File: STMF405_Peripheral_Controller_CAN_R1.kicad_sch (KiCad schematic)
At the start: 169 parts, among them J1 10155435-00011LF, SW1 EVP-AA602W, U1 AP63205WU, U2 AP63203WU, U3 STM32F405RGTx, U4 TJA1051TK-3, Y1 8MHz

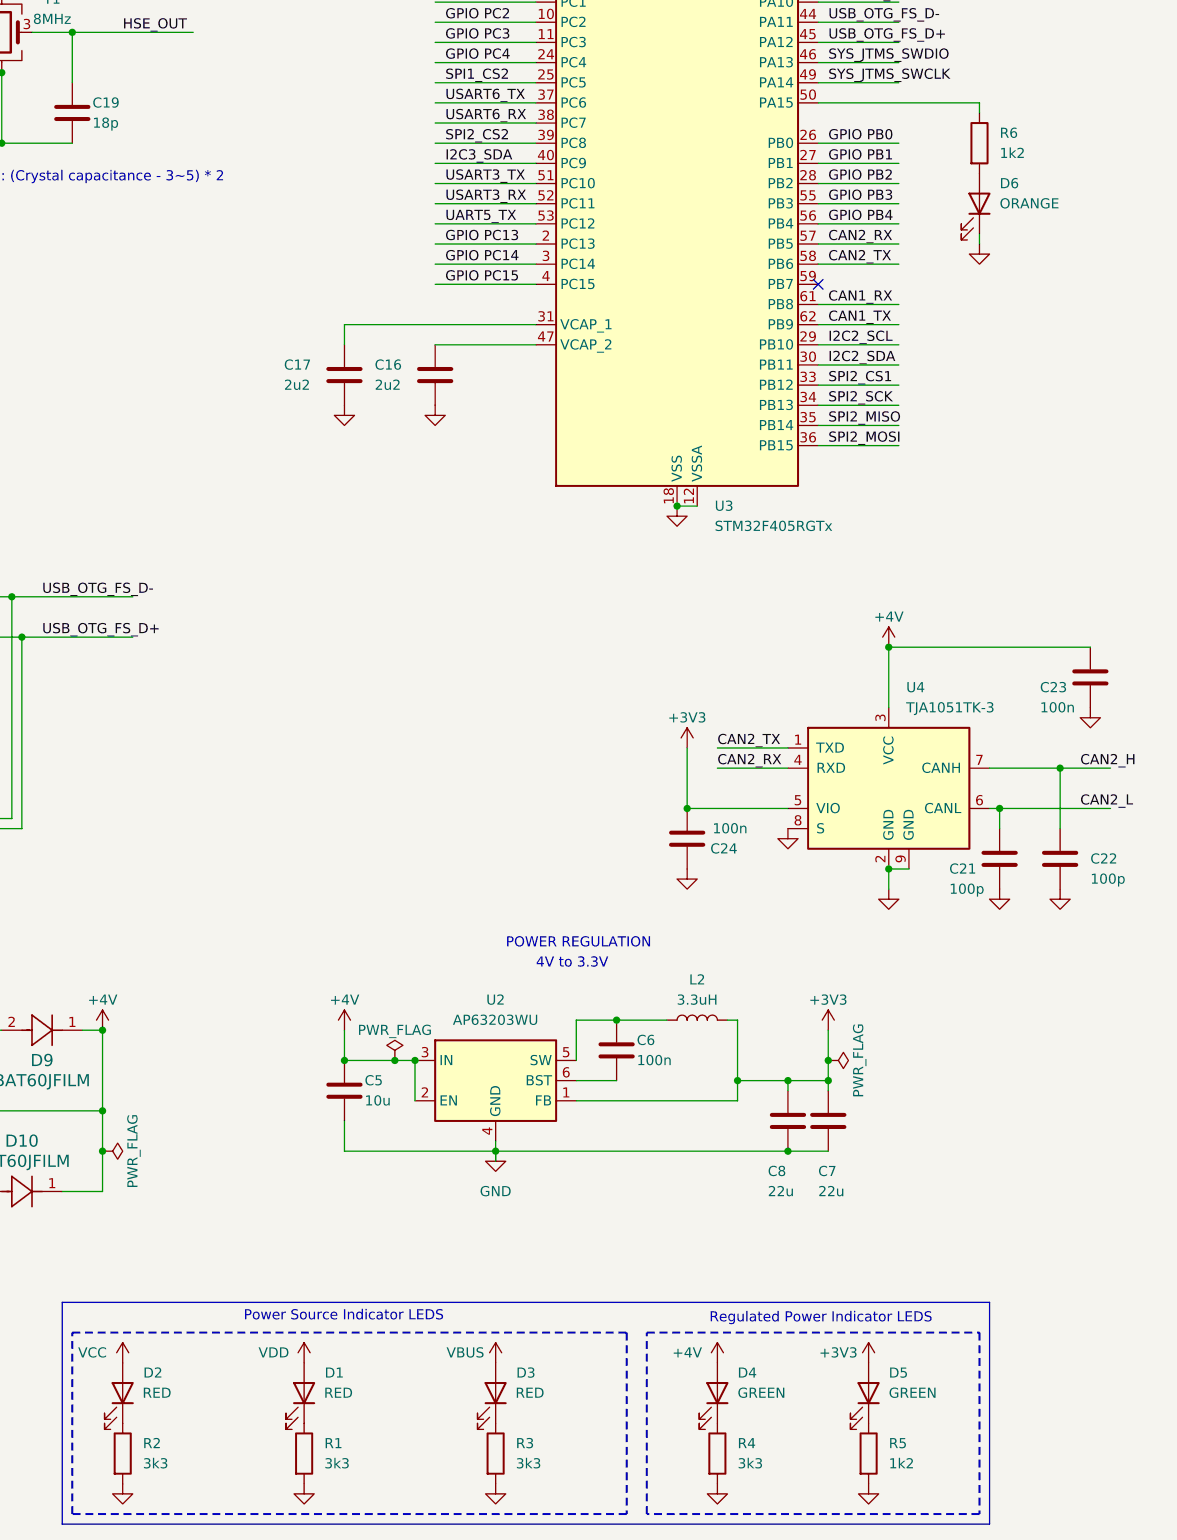
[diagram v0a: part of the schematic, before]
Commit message: cleanup resistors for LEDs, check rules and layout
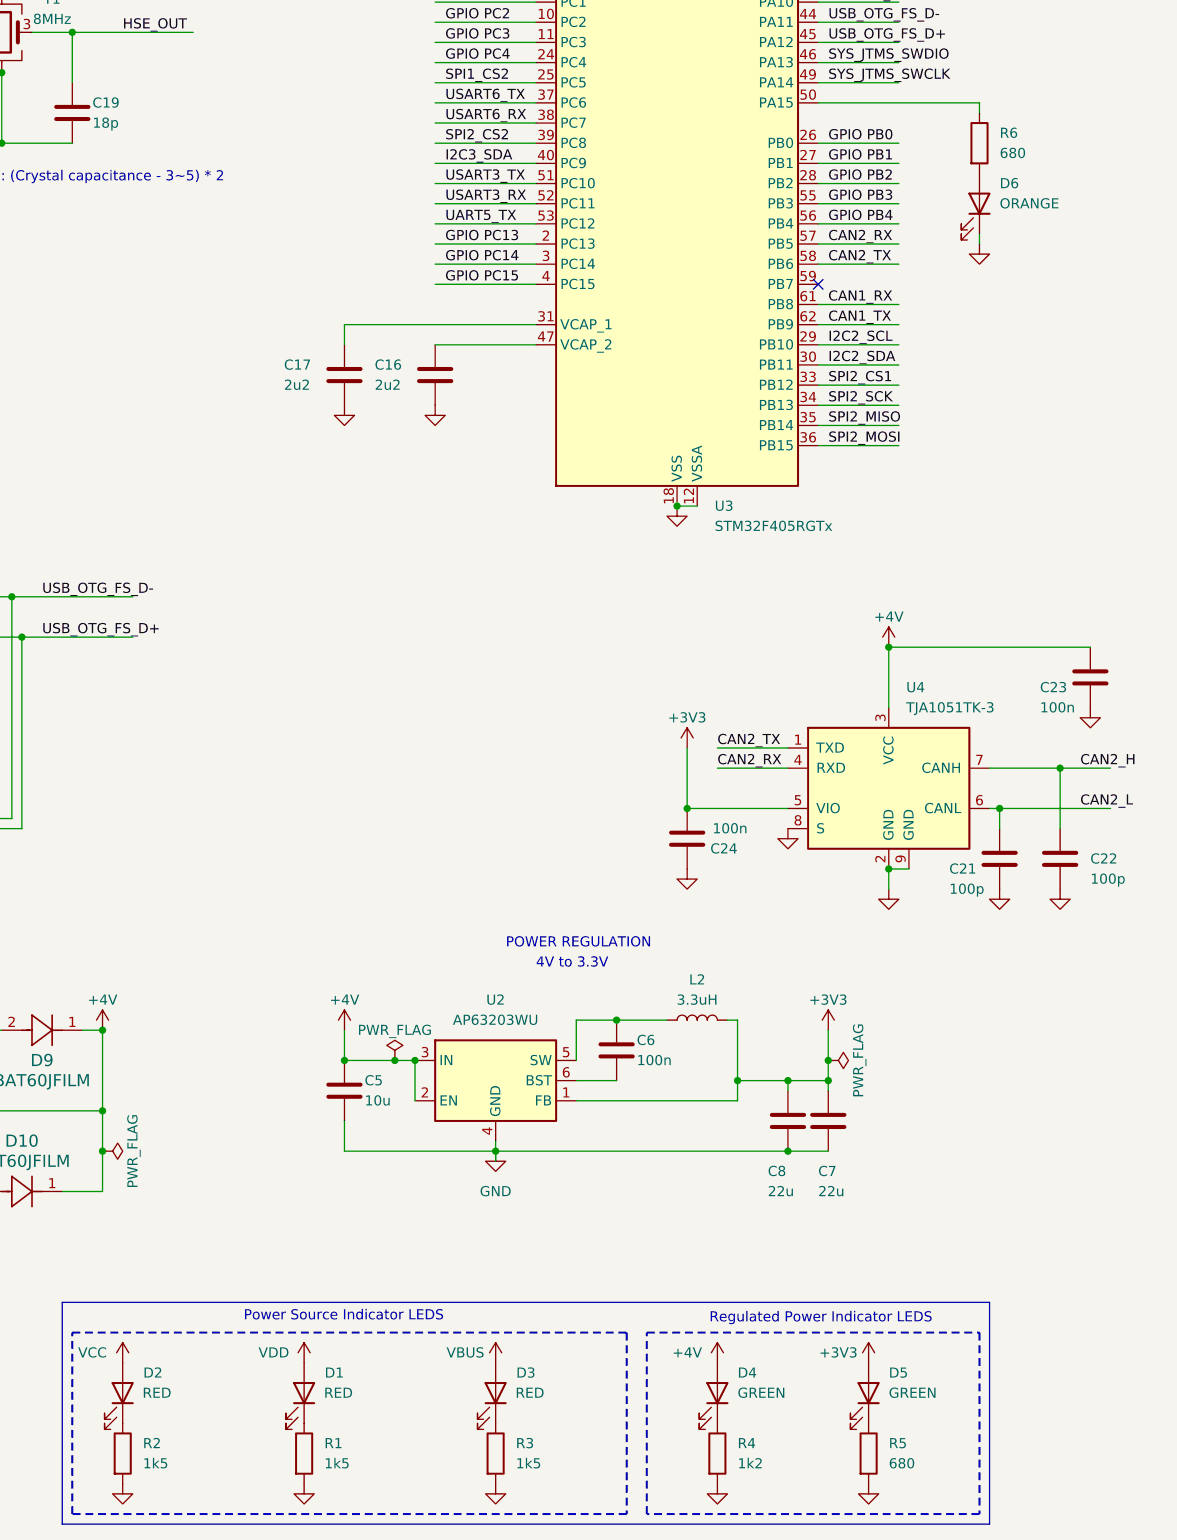
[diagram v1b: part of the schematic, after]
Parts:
- R1, R2, R3: value 3k3 -> 1k5; Part Number RC0402FR-073K3L -> RC0402FR-071K5L
- R4: value 3k3 -> 1k2; Part Number RC0402FR-073K3L -> RC0402FR-071K2L
- R5, R6: value 1k2 -> 680; Part Number RC0402FR-071K2L -> RC0402FR-07680RL
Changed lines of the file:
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@@
 			)
 		)
-		(property "Value" "1k2"
+		(property "Value" "680"
 			(at 259.08 274.3199 0)
 			(effects
@@
 			)
 		)
-		(property "Part Number" "RC0402FR-071K2L"
+		(property "Part Number" "RC0402FR-07680RL"
 			(at 256.54 273.05 0)
 			(effects
@@
 			)
 		)
-		(property "Value" "3k3"
+		(property "Value" "1k5"
 			(at 187.96 274.3199 0)
 			(effects
@@
 			)
 		)
-		(property "Part Number" "RC0402FR-073K3L"
+		(property "Part Number" "RC0402FR-071K5L"
 			(at 185.42 273.05 0)
 			(effects
@@
 			)
 		)
-		(property "Value" "3k3"
+		(property "Value" "1k2"
 			(at 240.03 274.3199 0)
 			(effects
@@
 			)
 		)
-		(property "Part Number" "RC0402FR-073K3L"
+		(property "Part Number" "RC0402FR-071K2L"
 			(at 237.49 273.05 0)
 			(effects
@@
 		(fields_autoplaced yes)
 		(property "Reference" "R3"
-			(at 212.09 271.78 0)
+			(at 212.09 271.7799 0)
 			(effects
 				(font
@@
 			)
 		)
-		(property "Value" "3k3"
-			(at 212.09 274.32 0)
+		(property "Value" "1k5"
+			(at 212.09 274.3199 0)
 			(effects
 				(font
@@
 			)
 		)
-		(property "Part Number" "RC0402FR-073K3L"
+		(property "Part Number" "RC0402FR-071K5L"
 			(at 209.55 273.05 0)
 			(effects
@@
 			)
 		)
-		(property "Value" "1k2"
+		(property "Value" "680"
 			(at 273.05 109.2199 0)
 			(effects
@@
 			)
 		)
-		(property "Part Number" "RC0402FR-071K2L"
+		(property "Part Number" "RC0402FR-07680RL"
 			(at 270.51 107.95 0)
 			(effects
@@
 			)
 		)
-		(property "Value" "3k3"
+		(property "Value" "1k5"
 			(at 165.1 274.3199 0)
 			(effects
@@
 			)
 		)
-		(property "Part Number" "RC0402FR-073K3L"
+		(property "Part Number" "RC0402FR-071K5L"
 			(at 162.56 273.05 0)
 			(effects
